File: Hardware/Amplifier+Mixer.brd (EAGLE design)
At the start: 140 x 140 mm, 182 parts, among them IC1 7812, IC2 7805, IC3 7912, IC4 OPA134PA, IC5 OPA134PA, IC6 MEGA8-AI, IC7 74HCT04, J1 +12AC, J10 FAN, J2 0V, J3 -12AC, J4 PE, J5 TERMINAL-BLOCK-2PLUG-IN, J6 TERMINAL-BLOCK-2PLUG-IN, J7 ENCODER, J8 DISPLAY, J9 USB, K1 RELAY-F40.52, K2 RELAY-F40.52, Q1 NPN, U1 LM1117-3.3, U2 10k, U3 10k, U4 10k, U5 10k, U6 TDA7498L, U7 10k, U8 10k, X1 RCA-4-CHANNEL, X2 JST-XH2, X3 ICSP

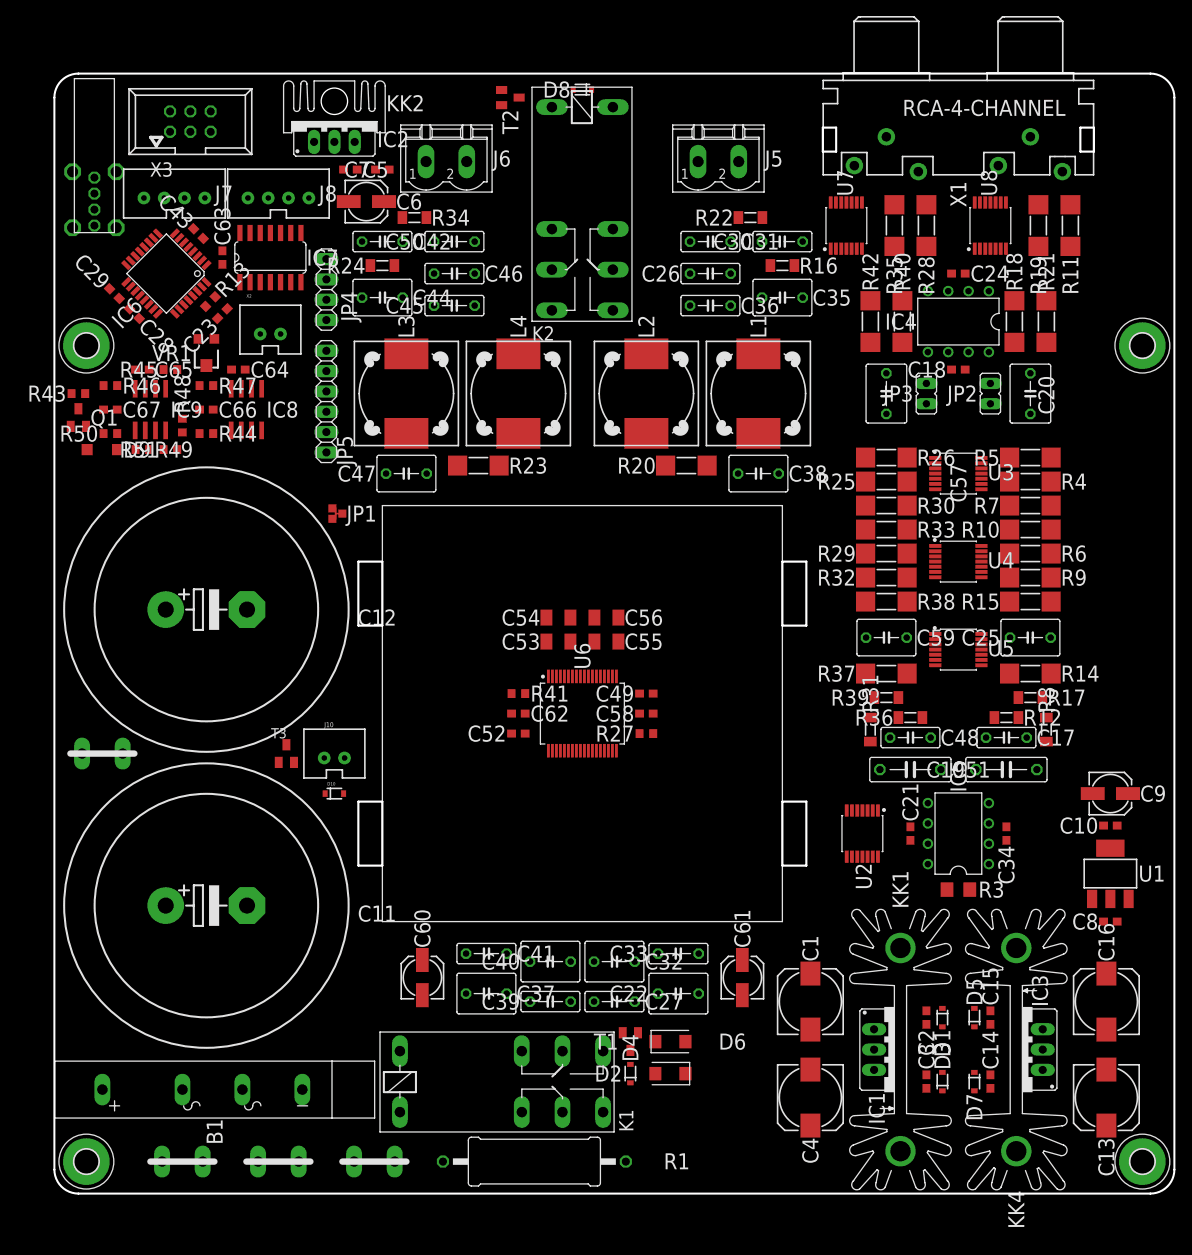
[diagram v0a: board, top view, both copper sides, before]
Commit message: consolidated some components to minimize BOM
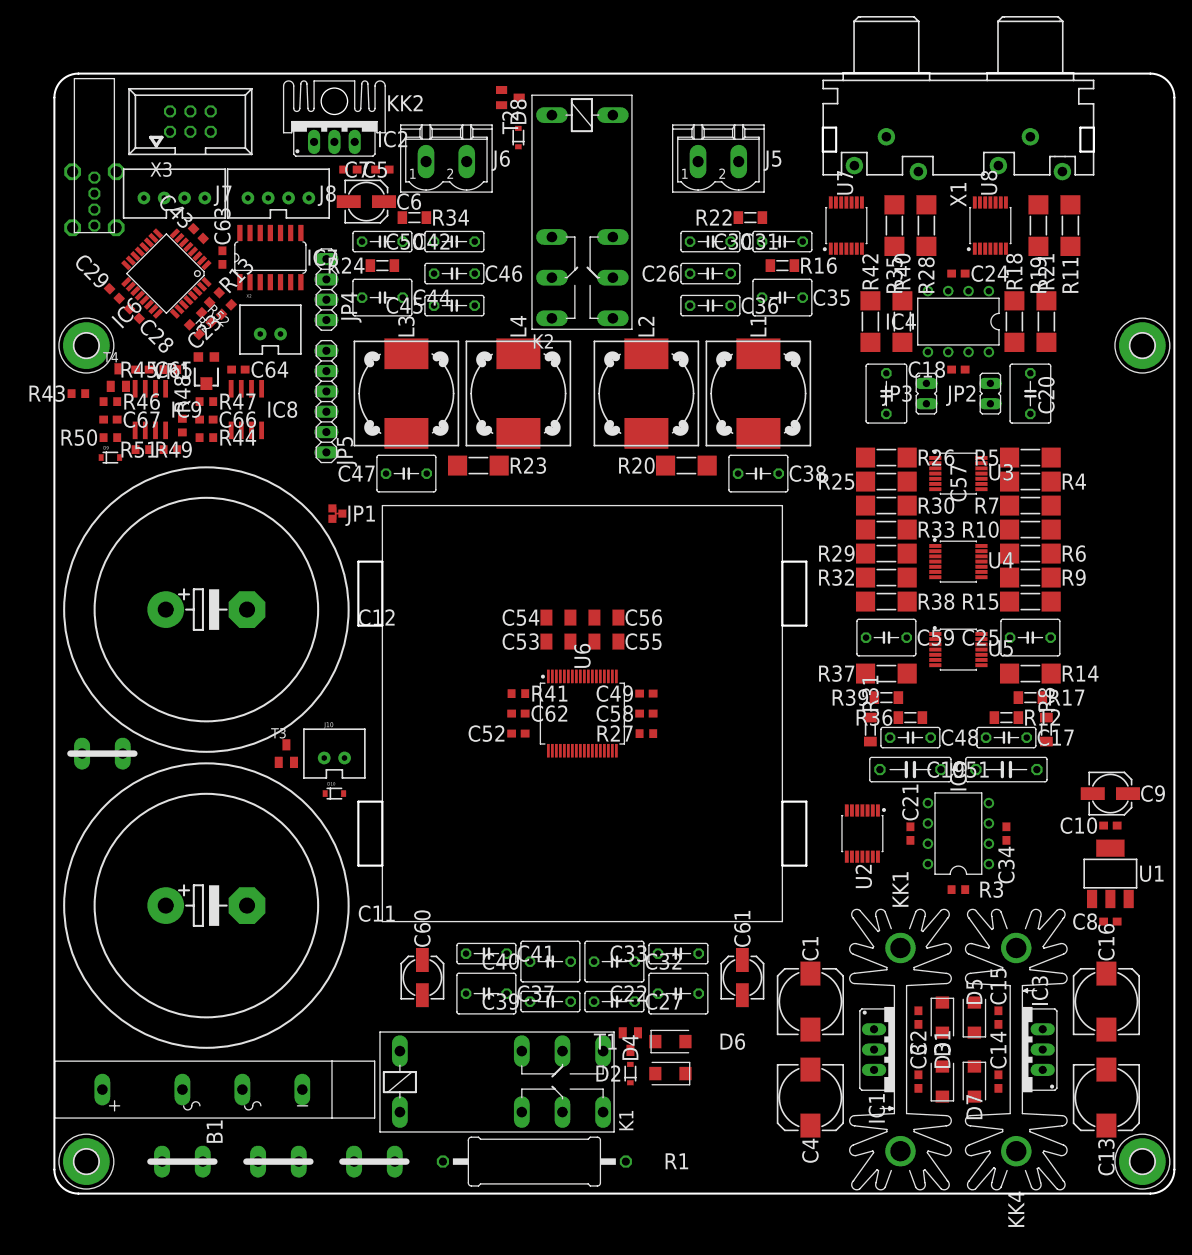
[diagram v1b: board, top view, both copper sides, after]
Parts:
- removed Q1: NPN, transistor-npn:SOT23-BEC
- added R2, R52: 4k7, rcl:R0603
- added T4: BC817, transistor:SOT23-BEC
- C66: value 104 -> 100n
- C67: value 105 -> 1µ
- D1, D3, D5, D7: value (none) -> 4007; device SparkFun-DiscreteSemi:SOD-323 -> Parts:SODFL5024X231
- D10, D4, D8: value (none) -> 1N4148
- D2, D6: value DIODE -> 4007
- D9: value (none) -> 1N4148; device diode:SOD123 -> SparkFun-DiscreteSemi:SOD-323
- J1: value +12AC -> 6MM
- J10: value FAN -> JST-XH2
- J2: value 0V -> 6MM
- J3: value -12AC -> 6MM
- J4: value PE -> 6MM
- JP2: value bypass AC couple right -> (none)
- JP3: value bypass AC couple left -> (none)
- K1, K2: value RELAY-F40.52 -> 12V 8A
- R3: device rcl:R1206 -> rcl:R0603
- T1, T2, T3: value (none) -> BC817
- X1: value RCA-4-CHANNEL -> (none)
- moved D8 10.0 mm to (58.0, 132.0), turned to 90 degrees
- moved VR1 2.25 mm to (19.0, 102.8)
- moved R46 2.00 mm to (7.00, 99.0)
- moved R47 2.00 mm to (19.0, 99.0)
- moved D9 1.41 mm to (7.00, 92.0)
- moved C66 1.25 mm to (19.0, 96.8)
- moved C67 1.25 mm to (7.00, 96.8)
- moved C14 1.00 mm to (118.0, 14.0)
- moved C15 1.00 mm to (118.0, 22.0)
- moved C2 1.00 mm to (108.0, 22.0)
- moved C3 1.00 mm to (108.0, 14.0)
- moved K2 1.00 mm to (66.0, 131.0)
- moved C23 0.71 mm to (21.5, 110.5)
- moved R13 0.71 mm to (20.0, 112.0)
- moved R44 0.50 mm to (19.0, 94.5)
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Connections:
- net +3V3: now also R2.2, R52.2
- net AUDIO_DETECT: now also T4.C; no longer Q1.C
- net DGND: now also T4.E; no longer Q1.E
- net N$37: now also T4.B; no longer Q1.B
- net SCL: now also R52.1
- net SDA: now also R2.1

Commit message: added order numbers for conrad and mouser as attributes of the parts
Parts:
- C1, C13: value 220µ -> 220µ 25V
- C16, C4: value 470µ -> 470µ 16V
- C6, C9: value 4.7µ -> 4.7µ 10V
- IC8, IC9: value (none) -> LM358D
- L1, L2, L3, L4: value 22µ 2.8A -> 22µ 2.2A
- VR1: value 10k -> 100k
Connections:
- removed net N$46: U7.8, X1.6
- removed net N$47: U8.8, X1.3
- removed net N$48: U8.7, X1.2
- removed net N$49: U7.7, X1.5
- net AGND: now also U7.7, U7.8; no longer U7.10, U7.5, U8.10, U8.5
- net N$40: now also U7.5, X1.6; no longer R11.1, U8.9
- net N$41: now also U7.10, X1.5; no longer R19.1, U8.6
- net N$42: now also U7.9; no longer U7.6
- net N$43: now also U7.6; no longer U7.9

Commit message: first routing pass
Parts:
- added JP6: PREAMP OUT, pinhead:2X03
- added R54, R55: 39k, rcl:R0603
- added S1: GAIN SELECT, switch-dil:DIP02YL
- C20: value 1µ -> DC COUPLE L
- JP2: value (none) -> DC COULE R
- JP3: value (none) -> DC COUPLE L
- JP5: value EXPANSION -> MIX OUT; device pinhead:1X06 -> pinhead:2X03
- X1: value (none) -> RCA-4-CHANNEL
- moved JP1 82.2 mm to (102.0, 36.0), flipped to the bottom, turned to 270 degrees
- moved JP5 80.5 mm to (113.0, 114.2), turned to 180 degrees
- moved J2 47.0 mm to (87.0, 4.00)
- moved C61 44.1 mm to (42.0, 24.0), turned to 180 degrees
- moved C17 23.2 mm to (122.0, 80.0), turned to 180 degrees
- moved C48 23.2 mm to (104.0, 80.0)
- moved R43 22.3 mm to (21.5, 112.5), turned to 135 degrees
- moved C19 20.5 mm to (119.0, 73.5)
- moved C51 20.5 mm to (107.0, 73.5)
- moved K1 20.0 mm to (67.0, 13.0), turned to 180 degrees
- moved R41 16.5 mm to (67.5, 49.0)
- moved C62 12.4 mm to (67.5, 52.0)
- moved D6 11.7 mm to (83.0, 9.00)
- moved X2 11.2 mm to (32.0, 98.0)
- moved R20 10.0 mm to (89.0, 90.0), turned to 0 degrees
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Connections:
- net N$57 renamed INNB
- net N$58 renamed INPB
- net N$59 renamed INNA
- net N$60 renamed INPA
- removed net N$88: IC6.24, JP5.5
- removed net N$89: IC6.25, JP5.4
- removed net N$90: IC6.26, JP5.3
- removed net N$91: K1.O1, R1.2
- new net AMP_MUTE_CL: R54.1, U6.21
- new net AMP_STBY_CL: R55.1, U6.20
- new net EQ_L: IC4.5, JP5.6
- new net EQ_R: IC4.3, JP5.2
- new net N$46: U8.5, X1.3
- new net N$47: U8.10, X1.2
- new net N$48: R19.1, U8.9
- new net N$49: R11.1, U8.6
- new net N$57: S1.3, U6.31
- new net N$58: S1.4, U6.30
- new net N$59: K1.O2, R1.2
- new net N$81: C22.1, JP6.1
- new net N$84: C37.1, JP6.5
- net +18V: now also K1.P1; no longer K1.P2
- net +3V3: now also S1.1, S1.2; no longer JP5.6, U6.30, U6.31
- net -18V: now also K1.P2; no longer K1.P1
- net AGND: now also JP5.3, JP5.4, JP6.3, JP6.4, U2.7, U2.8, U8.7, U8.8; no longer U2.10, U2.5
- net AMP_MUTE: now also R54.2; no longer U6.21
- net AMP_STBY: now also R55.2; no longer U6.20
- net DGND: no longer JP5.1, JP5.2, T1.E
- net EQ_OUT_L: now also U2.10; no longer U2.7
- net EQ_OUT_R: now also U2.5; no longer U2.8
- net GND: now also T1.E
- net L_OUT-: now also J6.1; no longer J6.2
- net MIX_L: now also JP5.5; no longer IC4.5
- net MIX_R: now also JP5.1; no longer IC4.3
- net N$27: now also K1.S2; no longer K1.S1
- net N$51: now also J6.2; no longer J6.1
- net N$53: now also K1.O1; no longer K1.S2
- net N$9: now also K1.S1; no longer K1.O2
- net PREAMP_OUT_L: now also JP6.6, U2.9; no longer C37.1, U2.6
- net PREAMP_OUT_R: now also JP6.2, U2.6; no longer C22.1, U2.9
- net SCL: now also IC7.1; no longer IC7.3
- net SCL_5V: now also IC7.12; no longer IC7.10
- net SDA: now also IC7.3; no longer IC7.1
- net SDA_5V: now also IC7.10; no longer IC7.12
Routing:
- net +3V3: track 0.00 -> 474.7 mm, vias 0 -> 26
- net +12V: track 0.00 -> 424.6 mm, vias 0 -> 6
- net DGND: track 0.00 -> 402.6 mm, vias 0 -> 31
- net SDA: track 0.00 -> 270.5 mm, vias 0 -> 7
- net SCL: track 0.00 -> 267.6 mm, vias 0 -> 13
- net AMP_PWR: track 0.00 -> 172.6 mm, vias 0 -> 4
- net MIX_R: track 0.00 -> 169.1 mm, vias 0 -> 2
- net MIX_L: track 0.00 -> 163.7 mm, vias 0 -> 2
- net -12V: track 0.00 -> 161.7 mm, vias 0 -> 3
- net +18V: track 0.00 -> 155.1 mm, vias 0 -> 9
- net -18V: track 0.00 -> 145.9 mm, vias 0 -> 13
- net AMP_MUTE: track 0.00 -> 126.9 mm, vias 0 -> 2
- net AMP_DIAG: track 0.00 -> 122.7 mm, vias 0 -> 2
- net AMP_STBY: track 0.00 -> 121.8 mm, vias 0 -> 2
- net +5V: track 0.00 -> 100.6 mm
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- added copper zone on layer 1, net +18V
- added copper zone on layer 1, net -18V
- added copper zone on layer 1, net AGND
- added copper zone on layer 16, net AGND
- added copper zone on layer 1, net DGND
- added copper zone on layer 16, net DGND
- added copper zone on layer 1, net GND
- added copper zone on layer 16, net GND
- added copper zone on layer 1, net PE
- added copper zone on layer 16, net PE
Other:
- outline, holes or cut-outs redrawn

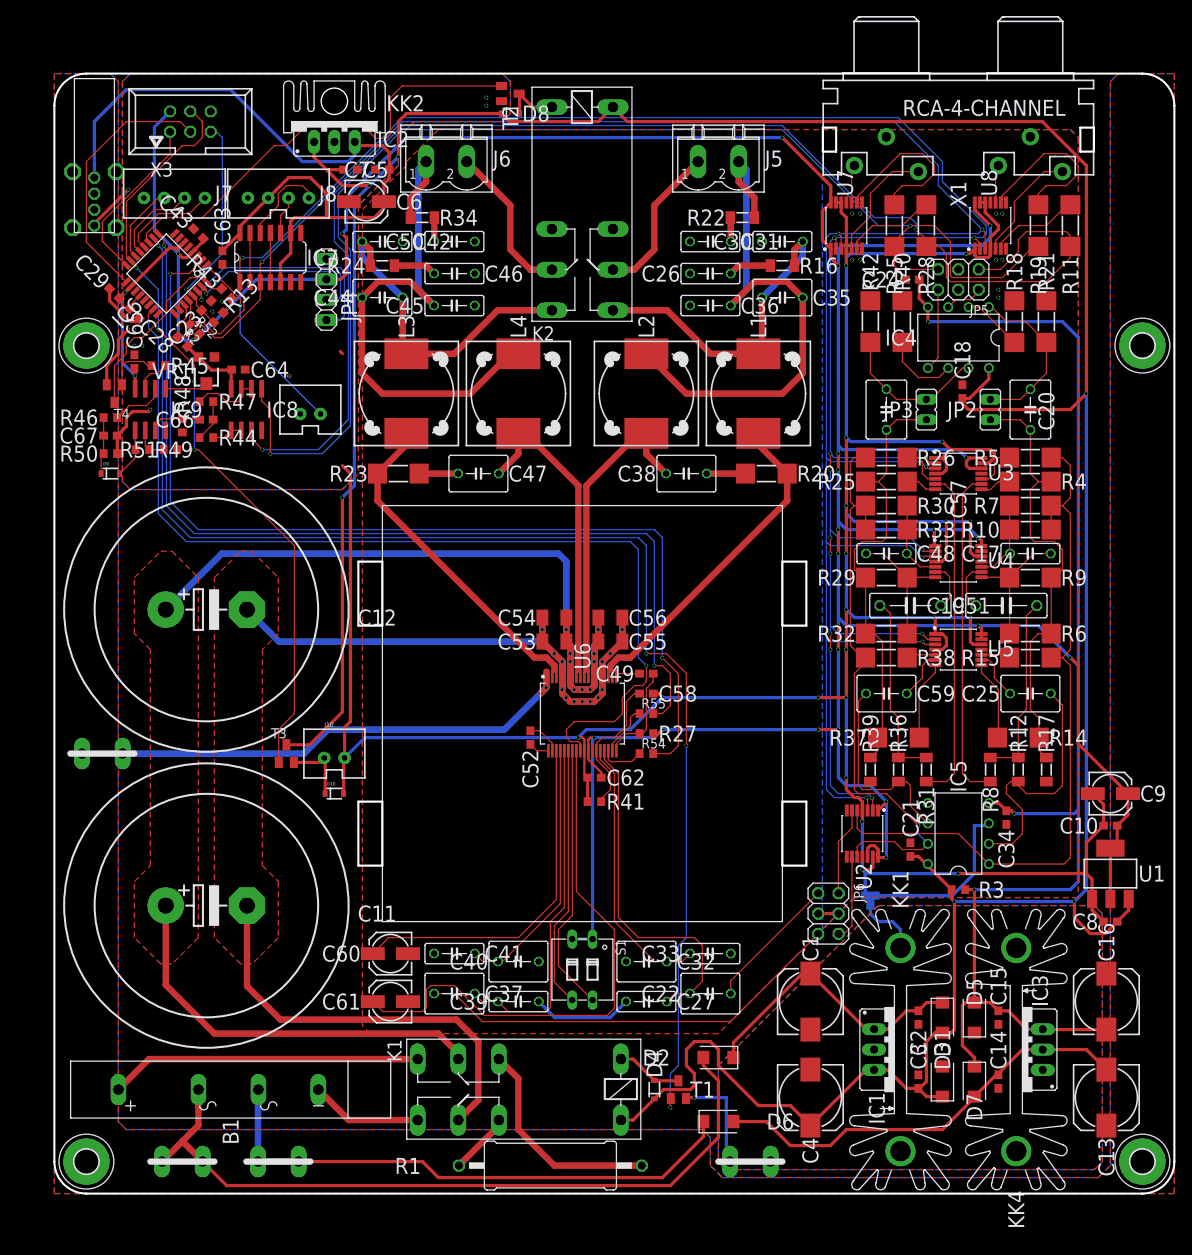
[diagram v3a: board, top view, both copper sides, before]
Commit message: first silkscreen placement pass
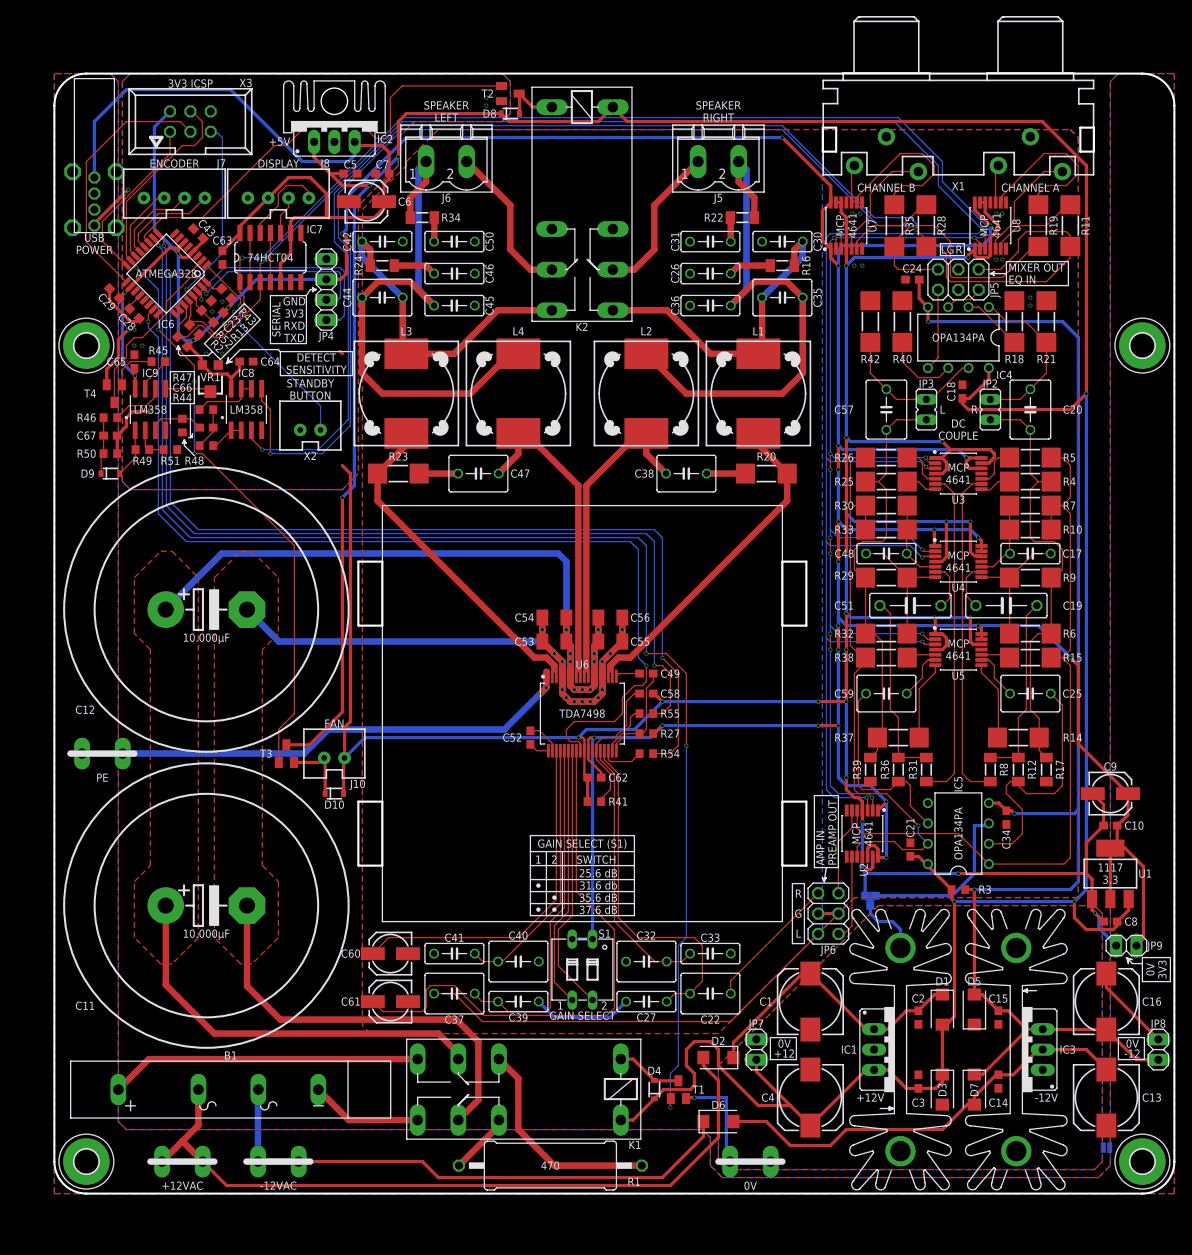
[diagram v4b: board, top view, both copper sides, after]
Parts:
- added JP10: PEGND, SparkFun-Jumpers:SMT-JUMPER_2_NO_NO-SILK
- added JP7, JP8, JP9: (no value), pinhead:1X02
- moved X2 2.00 mm to (32.0, 96.0)
- moved C64 1.41 mm to (24.0, 104.0)
- moved VR1 1.12 mm to (19.5, 101.8)
- moved C66 1.00 mm to (19.0, 95.8)
- moved D1 1.00 mm to (111.0, 23.0)
- moved D3 1.00 mm to (111.0, 13.0), turned to 270 degrees
- moved D5 1.00 mm to (115.0, 23.0)
- moved D7 1.00 mm to (115.0, 13.0)
- moved R44 1.00 mm to (19.0, 93.5)
- moved R47 1.00 mm to (19.0, 98.0)
- moved C5 0.50 mm to (37.0, 127.5)
- moved C7 0.50 mm to (41.0, 127.5)
- moved R45 0.50 mm to (13.0, 104.0)
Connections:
- net N$57 renamed GAIN1
- net N$58 renamed GAIN0
- net +12V: now also JP7.2
- net +3V3: now also JP9.2
- net -12V: now also JP8.2
- net DGND: now also JP9.1
- net GND: now also JP10.1, JP7.1, JP8.1
- net PE: now also JP10.2
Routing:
- net +3V3: track 474.7 -> 492.7 mm
- net GND: track 21.2 -> 32.1 mm
- net -12V: track 161.7 -> 168.3 mm
- net DGND: track 402.6 -> 407.7 mm, vias 31 -> 36
- net +12V: track 424.6 -> 428.5 mm
- net PWR_BTN: track 24.5 -> 26.5 mm
- net N$37: track 6.48 -> 5.98 mm
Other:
- board text added: "+12"
- board text added: "+12V"
- board text added: "+12VAC"
- board text added: "+5V"
- board text added: "-12"
- board text added: "-12V"
- board text added: "-12VAC"
- board text added: "0V"
- board text added: "1"
- board text added: "10.000µF"
- board text added: "1117 3.3"
- board text added: "2"
- board text added: "25.6 dB 31.6 db 35.6 dB 37.6 dB"
- board text added: "3V3"
- board text added: "3V3 ICSP"
- board text added: "470"
- board text added: "74HCT04"
- board text added: "AMP IN"
- board text added: "ATMEGA328"
- board text added: "CHANNEL A"
- board text added: "CHANNEL B"
- board text added: "DC COUPLE"
- board text added: "DETECT SENSITIVITY"
- board text added: "DISPLAY"
- board text added: "ENCODER"
- board text added: "EQ IN"
- board text added: "FAN"
- board text added: "G"
- board text added: "GAIN SELECT"
- board text added: "GAIN SELECT (S1)"
- board text added: "GND 3V3 RXD TXD"
- board text added: "L"
- board text added: "LM358"
- board text added: "MCP 4641"
- board text added: "MIXER OUT"
- board text added: "OPA134PA"
- board text added: "PE"
- board text added: "PE - GND REF"
- board text added: "PREAMP OUT"
- board text added: "R"
- board text added: "SERIAL"
- board text added: "SPEAKER LEFT"
- board text added: "SPEAKER RIGHT"
- board text added: "STANDBY BUTTON"
- board text added: "STAR GROUND"
- board text added: "SWITCH"
- board text added: "TDA7498"
- board text added: "USB POWER"
